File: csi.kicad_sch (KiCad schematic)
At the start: 5 parts, among them J6 Conn_FFC_WE_68715014022

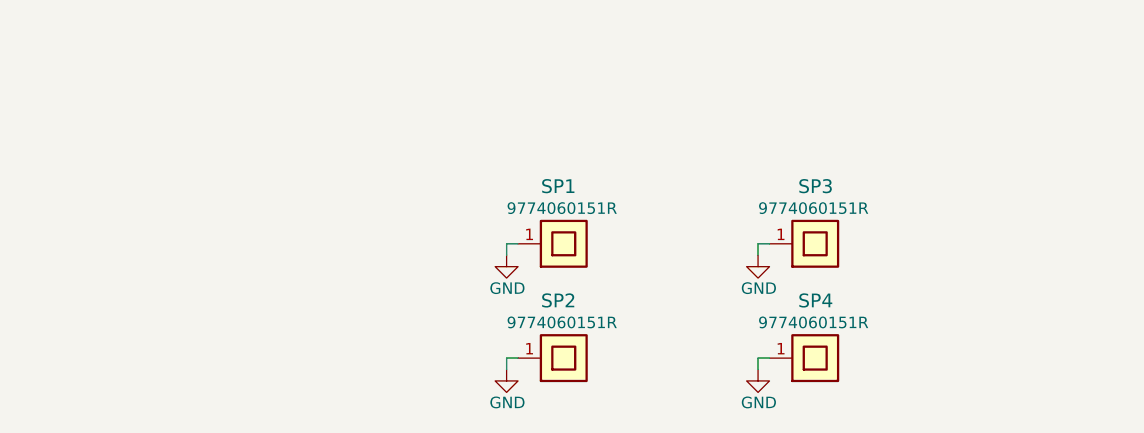
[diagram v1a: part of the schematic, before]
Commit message: Switch to micro-HDMI and widely-available parts for JLCPCB
- J2/J4: HDMI-A Molex 471511001 -> micro-HDMI (Type D) Molex 467651001,
  KiCad stock footprint. Symbol renumbered to the Type D pinout.
  D2/D0 fan out on F.Cu; D1/CLK drop to B.Cu via 0.15/0.30 mm vias in
  front of the inner pad row and rejoin the original routing, so the
  ESD-to-TC358743 routing is unchanged. Intra-pair skew re-matched to
  0.000 mm on all 8 pairs. DDC/HPD/CEC/5V re-routed for the new pinout.
- U3/U6: PCA9517ATP (HWSON8) -> PCA9517ADP (MSOP-8, same die), moved
  1.45 mm up into the space freed by the smaller connector.
- Y1/Y2: TXC 7C-27.000MBB-T -> HELE SSI027000E3CH; pads moved to the
  datasheet land (+-1.27 mm, previously +-1.9 mm).
- SP1-4: Wurth 9774060151R -> Sinhoo SMTSO2560CTJ; hole 3.7 -> 4.25 mm.
- IC2/IC4: TLV73312PDBVT -> TLV74312PDBVR (same pinout);
  IC1/IC3: TLV73325PDBVT -> TLV73325PDBVR (reel code).
- 470 pF, 4.7 uF, 2 k, 22 R: MPNs updated to in-stock equivalents.
- Design rules: min via diameter 0.40 -> 0.30 mm,
  min copper-to-edge clearance 0 -> 0.25 mm.

DRC: 0 unconnected, 0 schematic parity issues.

Co-Authored-By: Claude Opus 5.5 <noreply@anthropic.com>
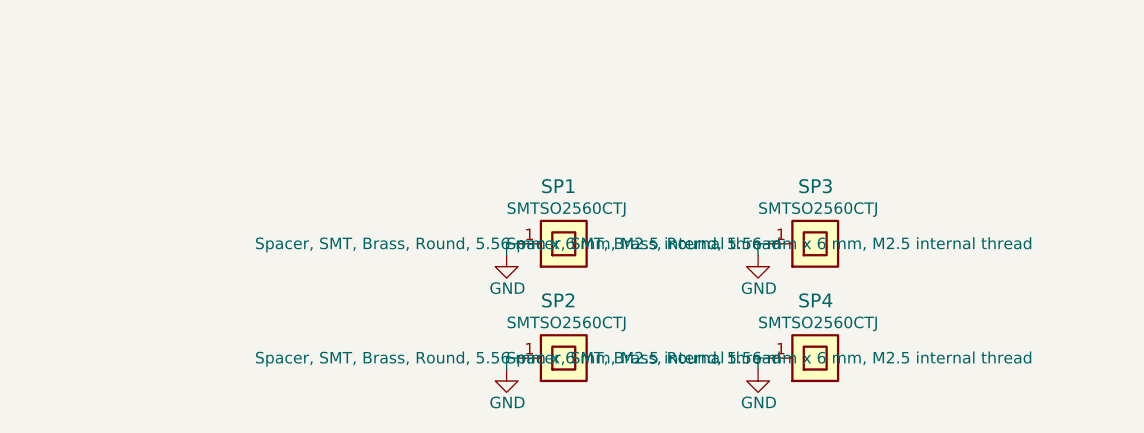
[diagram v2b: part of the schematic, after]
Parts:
- SP1, SP2, SP3, SP4: value Spacer_Drill3.7mm_H6mm_9774060151R -> Spacer_Drill4.25mm_H6mm_SMTSO2560CTJ; footprint antmicro-footprints:Spacer_Drill3.7mm_H6mm_9774060151R -> antmicro-footprints:Spacer_Drill4.25mm_H6mm_SMTSO2560CTJ; symbol antmicroMechanicalParts:Spacer_Drill3.7mm_H6mm_9774060151R -> antmicroMechanicalParts:Spacer_Drill4.25mm_H6mm_SMTSO2560CTJ; MPN 9774060151R -> SMTSO2560CTJ; Manufacturer Würth Elektronik -> Sinhoo
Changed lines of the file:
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@@
 	)
 	(symbol
-		(lib_id "antmicroMechanicalParts:Spacer_Drill3.7mm_H6mm_9774060151R")
+		(lib_id "antmicroMechanicalParts:Spacer_Drill4.25mm_H6mm_SMTSO2560CTJ")
 		(at 373.38 238.76 0)
 		(unit 1)
@@
 			)
 		)
-		(property "Value" "Spacer_Drill3.7mm_H6mm_9774060151R"
+		(property "Value" "Spacer_Drill4.25mm_H6mm_SMTSO2560CTJ"
 			(at 396.24 243.84 0)
 			(hide yes)
@@
 			)
 		)
-		(property "Footprint" "antmicro-footprints:Spacer_Drill3.7mm_H6mm_9774060151R"
+		(property "Footprint" "antmicro-footprints:Spacer_Drill4.25mm_H6mm_SMTSO2560CTJ"
 			(at 396.24 246.38 0)
 			(hide yes)
@@
 			)
 		)
-		(property "Datasheet" "https://www.we-online.com/components/products/datasheet/9774060151R.pdf"
+		(property "Datasheet" "https://www.lcsc.com/datasheet/lcsc_datasheet_2112061830_Sinhoo-SMTSO2560CTJ_C2916361.pdf"
 			(at 396.24 248.92 0)
 			(hide yes)
@@
 			)
 		)
-		(property "Description" ""
+		(property "Description" "Spacer, SMT, Brass, Round, 5.56 mm x 6 mm, M2.5 internal thread"
 			(at 373.38 238.76 0)
 			(show_name no)
@@
 			)
 		)
-		(property "Manufacturer" "Würth Elektronik"
+		(property "Manufacturer" "Sinhoo"
 			(at 396.24 251.46 0)
 			(hide yes)
@@
 			)
 		)
-		(property "MPN" "9774060151R"
+		(property "MPN" "SMTSO2560CTJ"
 			(at 372.11 235.585 0)
 			(show_name no)
@@
 	)
 	(symbol
-		(lib_id "antmicroMechanicalParts:Spacer_Drill3.7mm_H6mm_9774060151R")
+		(lib_id "antmicroMechanicalParts:Spacer_Drill4.25mm_H6mm_SMTSO2560CTJ")
 		(at 345.44 226.06 0)
 		(unit 1)
@@
 			)
 		)
-		(property "Value" "Spacer_Drill3.7mm_H6mm_9774060151R"
+		(property "Value" "Spacer_Drill4.25mm_H6mm_SMTSO2560CTJ"
 			(at 368.3 231.14 0)
 			(hide yes)
@@
 			)
 		)
-		(property "Footprint" "antmicro-footprints:Spacer_Drill3.7mm_H6mm_9774060151R"
+		(property "Footprint" "antmicro-footprints:Spacer_Drill4.25mm_H6mm_SMTSO2560CTJ"
 			(at 368.3 233.68 0)
 			(hide yes)
@@
 			)
 		)
-		(property "Datasheet" "https://www.we-online.com/components/products/datasheet/9774060151R.pdf"
+		(property "Datasheet" "https://www.lcsc.com/datasheet/lcsc_datasheet_2112061830_Sinhoo-SMTSO2560CTJ_C2916361.pdf"
 			(at 368.3 236.22 0)
 			(hide yes)
@@
 			)
 		)
-		(property "Description" ""
+		(property "Description" "Spacer, SMT, Brass, Round, 5.56 mm x 6 mm, M2.5 internal thread"
 			(at 345.44 226.06 0)
 			(show_name no)
@@
 			)
 		)
-		(property "Manufacturer" "Würth Elektronik"
+		(property "Manufacturer" "Sinhoo"
 			(at 368.3 238.76 0)
 			(hide yes)
@@
 			)
 		)
-		(property "MPN" "9774060151R"
+		(property "MPN" "SMTSO2560CTJ"
 			(at 344.17 222.885 0)
 			(show_name no)
@@
 	)
 	(symbol
-		(lib_id "antmicroMechanicalParts:Spacer_Drill3.7mm_H6mm_9774060151R")
+		(lib_id "antmicroMechanicalParts:Spacer_Drill4.25mm_H6mm_SMTSO2560CTJ")
 		(at 373.38 226.06 0)
 		(unit 1)
@@
 			)
 		)
-		(property "Value" "Spacer_Drill3.7mm_H6mm_9774060151R"
+		(property "Value" "Spacer_Drill4.25mm_H6mm_SMTSO2560CTJ"
 			(at 396.24 231.14 0)
 			(hide yes)
@@
 			)
 		)
-		(property "Footprint" "antmicro-footprints:Spacer_Drill3.7mm_H6mm_9774060151R"
+		(property "Footprint" "antmicro-footprints:Spacer_Drill4.25mm_H6mm_SMTSO2560CTJ"
 			(at 396.24 233.68 0)
 			(hide yes)
@@
 			)
 		)
-		(property "Datasheet" "https://www.we-online.com/components/products/datasheet/9774060151R.pdf"
+		(property "Datasheet" "https://www.lcsc.com/datasheet/lcsc_datasheet_2112061830_Sinhoo-SMTSO2560CTJ_C2916361.pdf"
 			(at 396.24 236.22 0)
 			(hide yes)
@@
 			)
 		)
-		(property "Description" ""
+		(property "Description" "Spacer, SMT, Brass, Round, 5.56 mm x 6 mm, M2.5 internal thread"
 			(at 373.38 226.06 0)
 			(show_name no)
@@
 			)
 		)
-		(property "Manufacturer" "Würth Elektronik"
+		(property "Manufacturer" "Sinhoo"
 			(at 396.24 238.76 0)
 			(hide yes)
@@
 			)
 		)
-		(property "MPN" "9774060151R"
+		(property "MPN" "SMTSO2560CTJ"
 			(at 372.11 222.885 0)
 			(show_name no)
@@
 	)
 	(symbol
-		(lib_id "antmicroMechanicalParts:Spacer_Drill3.7mm_H6mm_9774060151R")
+		(lib_id "antmicroMechanicalParts:Spacer_Drill4.25mm_H6mm_SMTSO2560CTJ")
 		(at 345.44 238.76 0)
 		(unit 1)
@@
 			)
 		)
-		(property "Value" "Spacer_Drill3.7mm_H6mm_9774060151R"
+		(property "Value" "Spacer_Drill4.25mm_H6mm_SMTSO2560CTJ"
 			(at 368.3 243.84 0)
 			(hide yes)
@@
 			)
 		)
-		(property "Footprint" "antmicro-footprints:Spacer_Drill3.7mm_H6mm_9774060151R"
+		(property "Footprint" "antmicro-footprints:Spacer_Drill4.25mm_H6mm_SMTSO2560CTJ"
 			(at 368.3 246.38 0)
 			(hide yes)
@@
 			)
 		)
-		(property "Datasheet" "https://www.we-online.com/components/products/datasheet/9774060151R.pdf"
+		(property "Datasheet" "https://www.lcsc.com/datasheet/lcsc_datasheet_2112061830_Sinhoo-SMTSO2560CTJ_C2916361.pdf"
 			(at 368.3 248.92 0)
 			(hide yes)
@@
 			)
 		)
-		(property "Description" ""
+		(property "Description" "Spacer, SMT, Brass, Round, 5.56 mm x 6 mm, M2.5 internal thread"
 			(at 345.44 238.76 0)
 			(show_name no)
@@
 			)
 		)
-		(property "Manufacturer" "Würth Elektronik"
+		(property "Manufacturer" "Sinhoo"
 			(at 368.3 251.46 0)
 			(hide yes)
@@
 			)
 		)
-		(property "MPN" "9774060151R"
+		(property "MPN" "SMTSO2560CTJ"
 			(at 344.17 235.585 0)
 			(show_name no)
